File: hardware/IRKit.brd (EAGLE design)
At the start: 54 x 56 mm, 71 parts, among them CN1 USB-CONNECTORMICROB, IC1 ATMEGA32U4AU, IC2 TLV70233DBVT, IC3 LM386MM-1, IC4 GS1011MXXS, SW1 EVQPUJ02K, T1 2SD1781K, T2 BSS138

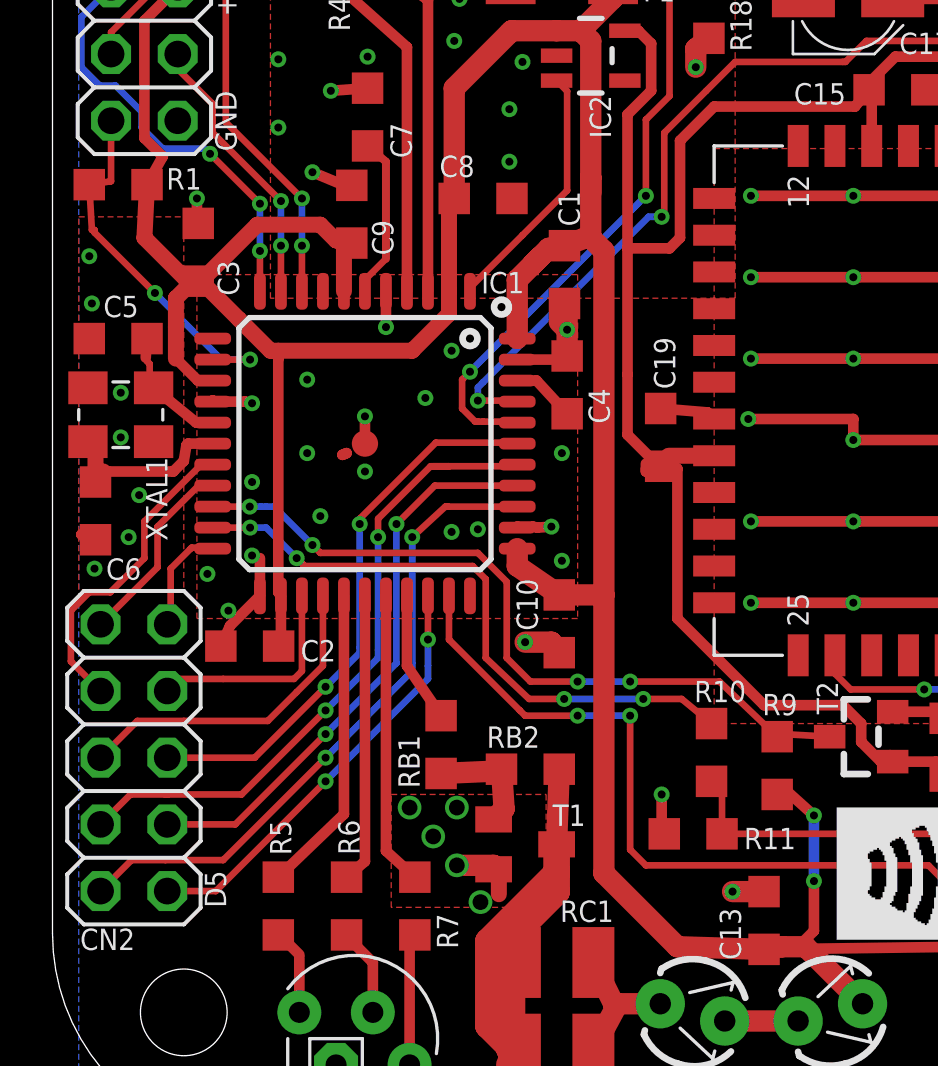
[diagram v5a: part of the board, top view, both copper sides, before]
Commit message: crystal should use the exact recommended board pattern
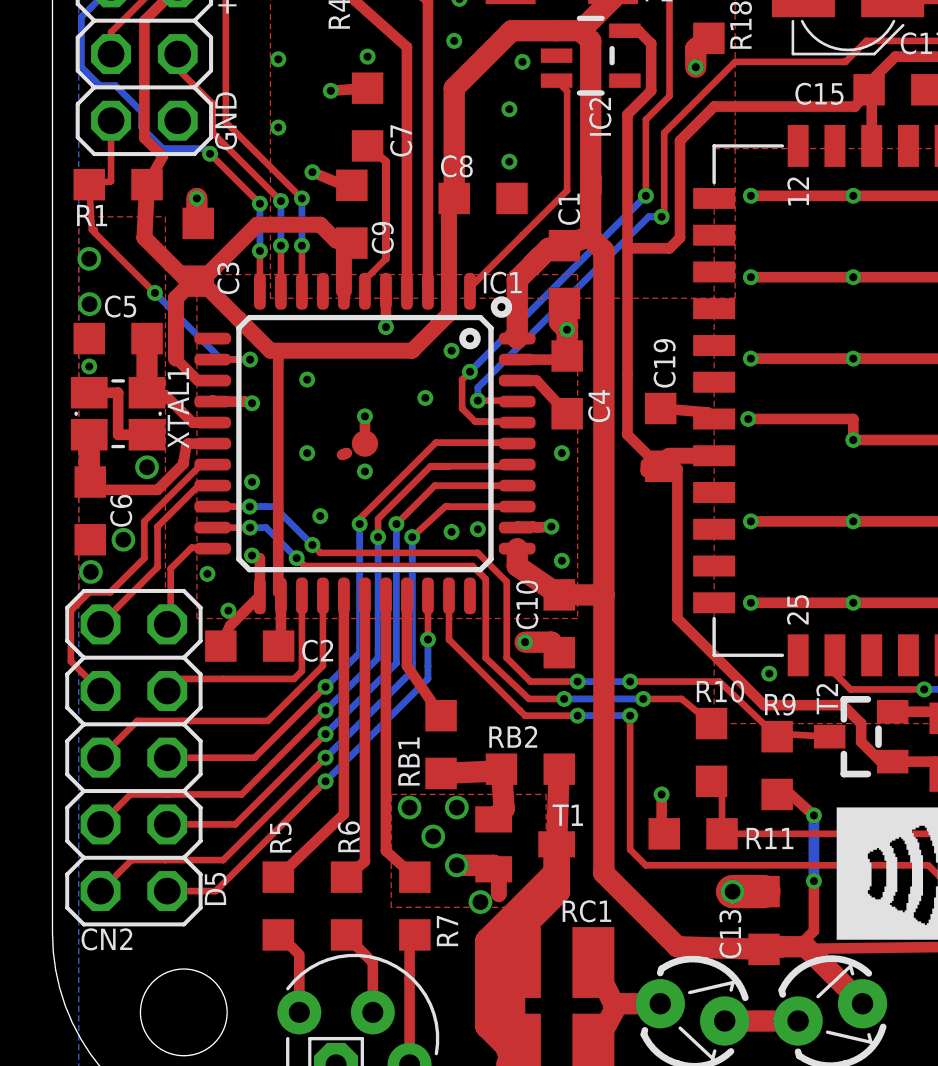
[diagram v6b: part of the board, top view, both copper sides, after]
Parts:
- moved C6 0.20 mm to (1.44, 24.1)
- moved XTAL1 0.11 mm to (2.50, 27.8)
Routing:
- net GND: track 187.2 -> 190.6 mm
- net XTAL2: track 7.30 -> 7.91 mm
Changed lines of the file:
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@@
 </element>
 <element name="R1" library="my" package="SMD2012" value="10k" x="2.5" y="36.525" smashed="yes">
-<attribute name="NAME" x="4.338" y="36.341" size="0.8128" layer="25"/>
+<attribute name="NAME" x="0.838" y="34.941" size="0.8128" layer="25"/>
 <attribute name="VALUE" x="0.638" y="35.739" size="0.8128" layer="27"/>
 </element>
@@
 <attribute name="VALUE" x="1.738" y="28.3765" size="0.8128" layer="27"/>
 </element>
-<element name="C6" library="my" package="SMD2012" value="22pF" x="1.6375" y="24.1" smashed="yes" rot="R90">
-<attribute name="NAME" x="2.038" y="21.4785" size="0.8128" layer="25"/>
-<attribute name="VALUE" x="3.9235" y="23.338" size="0.8128" layer="27" rot="R90"/>
+<element name="C6" library="my" package="SMD2012" value="22pF" x="1.4375" y="24.1" smashed="yes" rot="R90">
+<attribute name="NAME" x="3.0215" y="23.438" size="0.8128" layer="25" rot="R90"/>
+<attribute name="VALUE" x="3.7235" y="23.338" size="0.8128" layer="27" rot="R90"/>
 </element>
 <element name="C14" library="my" package="SMD2012" value="4.7uF" x="43.45" y="6.65" smashed="yes" rot="R180">
@@
 <attribute name="NAME" x="22.495" y="43.505" size="0.8128" layer="25"/>
 <attribute name="VALUE" x="17.495" y="41.925" size="1.27" layer="27"/>
-</element>
-<element name="XTAL1" library="my" package="CRYSTAL-3.2-2.5" value="16MHz" x="2.6" y="27.7625" smashed="yes">
-<attribute name="NAME" x="3.5625" y="26.15" size="0.8128" layer="25" rot="R270"/>
-<attribute name="VALUE" x="1" y="25.5125" size="0.8128" layer="27"/>
 </element>
 <element name="R10" library="my" package="SMD2012" value="2.2k" x="25.1" y="14.9" smashed="yes" rot="R90">
@@
 <attribute name="NAME" x="15.9" y="49.2" size="0.8128" layer="25"/>
 <attribute name="VALUE" x="15.9" y="46.6" size="1.016" layer="27"/>
+</element>
+<element name="XTAL1" library="my" package="CRYSTAL-3.2-2.5" value="16MHz" x="2.5" y="27.8" smashed="yes">
+<attribute name="NAME" x="5.2" y="26.45" size="0.8128" layer="25" rot="R90"/>
+<attribute name="VALUE" x="0.9" y="25.55" size="1.27" layer="27"/>
 </element>
 </elements>
@@
 <contactref element="ICSP" pad="6"/>
 <contactref element="IR-RECEIVER" pad="2"/>
-<polygon width="0.4064" layer="16" isolate="0.254">
+<polygon width="0.8128" layer="16" isolate="0.254">
 <vertex x="1" y="1"/>
 <vertex x="1" y="55"/>
@@
 <contactref element="CN1" pad="S5"/>
 <contactref element="CN1" pad="S6"/>
-<contactref element="XTAL1" pad="2"/>
 <via x="11.9" y="27.7" extent="1-16" drill="0.3048"/>
 <wire x1="11.9" y1="26.6625" x2="11.9" y2="27.7" width="0.4064" layer="1"/>
@@
 <contactref element="IC1" pad="43"/>
 <contactref element="C6" pad="1"/>
-<contactref element="XTAL1" pad="4"/>
 <contactref element="C11" pad="2"/>
 <contactref element="C14" pad="2"/>
 <wire x1="21.5" y1="51.8" x2="21.3" y2="51.7" width="0.4064" layer="1"/>
 <wire x1="24.9" y1="52" x2="24.996" y2="52.0735" width="0.4064" layer="1"/>
-<wire x1="1.5" y1="23.3" x2="1.6375" y2="23" width="0.4064" layer="1"/>
+<wire x1="1.5" y1="23.3" x2="1.4375" y2="23" width="0.4064" layer="1"/>
 <wire x1="25.2" y1="52" x2="24.996" y2="52.0735" width="0.4064" layer="1"/>
-<via x="2.9" y="23.1" extent="1-16" drill="0.3048"/>
+<via x="2.7" y="23" extent="1-16" drill="0.6"/>
 <wire x1="18.4625" y1="23.4625" x2="19" y2="23.5" width="0.4064" layer="1"/>
 <wire x1="18.3" y1="23.5" x2="17.7" y2="23.5" width="0.4064" layer="1"/>
@@
 <wire x1="11.1" y1="36.5" x2="9.9" y2="37" width="0.4064" layer="1"/>
 <wire x1="12" y1="40.2" x2="10.6" y2="40.1" width="0.4064" layer="1"/>
-<wire x1="1.5" y1="23.3" x2="1.6375" y2="23" width="0.4064" layer="1"/>
-<polygon width="0.4064" layer="1">
+<wire x1="1.5" y1="23.3" x2="1.4375" y2="23" width="0.4064" layer="1"/>
+<polygon width="0.8128" layer="1">
 <vertex x="1" y="35.3"/>
-<vertex x="5" y="35.3"/>
-<vertex x="5" y="21.1"/>
+<vertex x="4.3" y="35.3"/>
+<vertex x="4.3" y="21.1"/>
 <vertex x="1" y="21.1"/>
 </polygon>
-<via x="1.4" y="33.8" extent="1-16" drill="0.3048"/>
-<via x="1.5" y="32" extent="1-16" drill="0.3048"/>
-<via x="2.6" y="26.9" extent="1-16" drill="0.3048"/>
-<via x="3.3" y="24.7" extent="1-16" drill="0.3048"/>
-<via x="1.6" y="21.9" extent="1-16" drill="0.3048"/>
+<via x="1.4" y="33.7" extent="1-16" drill="0.6"/>
+<via x="1.4125" y="31.975" extent="1-16" drill="0.6"/>
+<via x="1.4625" y="21.775" extent="1-16" drill="0.6"/>
 <polygon width="0.4064" layer="1" isolate="0.254">
 <vertex x="5.5" y="33.1"/>
@@
 <wire x1="19.6" y1="30" x2="19.4625" y2="29.8625" width="0.8128" layer="1"/>
 <wire x1="19.4625" y1="29.8625" x2="17.7" y2="29.8625" width="0.4064" layer="1"/>
-<wire x1="1.1" y1="23.2" x2="1.6375" y2="23" width="0.4064" layer="1"/>
-<wire x1="1.1" y1="23.2" x2="1.6375" y2="23" width="0.4064" layer="1"/>
+<wire x1="1.1" y1="23.2" x2="1.4375" y2="23" width="0.4064" layer="1"/>
+<wire x1="1.1" y1="23.2" x2="1.4375" y2="23" width="0.4064" layer="1"/>
 <via x="5.5" y="36" extent="1-16" drill="0.3048"/>
-<wire x1="5.5" y1="36" x2="5.5" y2="35" width="0.4064" layer="1"/>
 <wire x1="5.5" y1="35" x2="5.55" y2="35.05" width="0.4064" layer="1"/>
 <wire x1="19.5" y1="32" x2="19.6" y2="31.8" width="0.8128" layer="1"/>
@@
 <wire x1="42.4" y1="20.6" x2="42.2" y2="20.6" width="0.4064" layer="1"/>
 <via x="17.9" y="41.2" extent="1-16" drill="0.3048"/>
-<via x="2.6" y="28.6" extent="1-16" drill="0.3048"/>
 <contactref element="R16" pad="1"/>
 <contactref element="R18" pad="2"/>
@@
 <contactref element="C13" pad="2"/>
 <contactref element="V3" pad="2"/>
-<via x="25.9" y="9.6" extent="1-16" drill="0.3048"/>
+<via x="25.9" y="9.6" extent="1-16" drill="0.6"/>
 <wire x1="18" y1="19.1" x2="19" y2="19.1" width="0.8128" layer="1"/>
 <wire x1="19" y1="19.1" x2="19.3" y2="18.7" width="0.8128" layer="1"/>
@@
 <wire x1="42.9" y1="7" x2="42.35" y2="6.65" width="0.4064" layer="1"/>
 <via x="15.4" y="12.8" extent="1-16" drill="0.6"/>
-<wire x1="25.9" y1="9.6" x2="27.1" y2="9.6" width="0.8128" layer="1"/>
 <via x="23.2" y="13.3" extent="1-16" drill="0.3048"/>
 <wire x1="23.3" y1="11.8" x2="23.2" y2="12.1" width="0.4064" layer="1"/>
@@
 <via x="16.3" y="9.2" extent="1-16" drill="0.6"/>
 <via x="14.5" y="11.7" extent="1-16" drill="0.6"/>
+<via x="3.6" y="25.7625" extent="1-16" drill="0.6"/>
+<contactref element="XTAL1" pad="2"/>
+<contactref element="XTAL1" pad="4"/>
+<via x="1.4" y="29.6" extent="1-16" drill="0.3048"/>
+<wire x1="5.5" y1="35" x2="5.5" y2="36" width="0.8128" layer="1"/>
+<wire x1="27.1" y1="9.6" x2="25.9" y2="9.6" width="1.27" layer="1"/>
+<via x="27.3" y="17.9" extent="1-16" drill="0.3048"/>
+<wire x1="1.4" y1="28.6" x2="2.5" y2="28.6" width="0.4064" layer="1"/>
+<wire x1="2.5" y1="28.6" x2="2.5" y2="27" width="0.4064" layer="1"/>
+<wire x1="2.5" y1="27" x2="3.6" y2="27" width="0.4064" layer="1"/>
 </signal>
 <signal name="N$10">
@@
 </signal>
 <signal name="XTAL1">
-<contactref element="XTAL1" pad="3"/>
 <contactref element="C5" pad="2"/>
 <contactref element="IC1" pad="16"/>
-<wire x1="6.1" y1="27.4625" x2="5.475" y2="27.4625" width="0.4064" layer="1"/>
-<wire x1="5.475" y1="27.4625" x2="3.85" y2="28.7875" width="0.4064" layer="1"/>
-<wire x1="3.55" y1="29.9375" x2="3.6" y2="30.6625" width="0.4064" layer="1"/>
-<wire x1="3.7" y1="29.7" x2="3.6" y2="29.8" width="0.254" layer="1"/>
-<wire x1="3.7" y1="28.9" x2="3.7" y2="29.7" width="0.254" layer="1"/>
-<wire x1="3.6" y1="29.8" x2="3.6" y2="30.6625" width="0.254" layer="1"/>
-<wire x1="3.7" y1="28.9" x2="3.85" y2="28.7875" width="0.254" layer="1"/>
+<contactref element="XTAL1" pad="3"/>
+<wire x1="3.6" y1="30.6625" x2="3.6" y2="28.7" width="0.8128" layer="1"/>
+<wire x1="3.6" y1="28.7" x2="3.6" y2="28.6" width="0.8128" layer="1"/>
+<wire x1="6.1" y1="27.4625" x2="5.3375" y2="27.4625" width="0.4064" layer="1"/>
+<wire x1="5.3375" y1="27.4625" x2="4.3" y2="28.5" width="0.4064" layer="1"/>
+<wire x1="4.3" y1="28.5" x2="3.8" y2="28.5" width="0.4064" layer="1"/>
+<wire x1="3.8" y1="28.5" x2="3.6" y2="28.6" width="0.4064" layer="1"/>
 </signal>
 <signal name="XTAL2">
 <contactref element="C6" pad="2"/>
 <contactref element="IC1" pad="17"/>
-<contactref element="XTAL1" pad="1"/>
 <wire x1="6.1" y1="26.6625" x2="5.1625" y2="26.6625" width="0.4064" layer="1"/>
 <wire x1="5.1625" y1="26.6625" x2="5.1" y2="26.6" width="0.4064" layer="1"/>
 <wire x1="5.1" y1="26.6" x2="5" y2="26" width="0.4064" layer="1"/>
-<wire x1="5" y1="26" x2="4.6" y2="25.6" width="0.4064" layer="1"/>
-<wire x1="4.6" y1="25.6" x2="1.9375" y2="25.6" width="0.4064" layer="1"/>
-<wire x1="1.35" y1="26.7375" x2="1.6375" y2="26.45" width="0.6096" layer="1"/>
-<wire x1="1.6375" y1="26.45" x2="1.6375" y2="25.2" width="0.6096" layer="1"/>
-<wire x1="1.9375" y1="25.6" x2="1.6" y2="25.2625" width="0.6096" layer="1"/>
-<wire x1="1.7" y1="25.1" x2="1.6375" y2="25.2" width="0.254" layer="1"/>
-<wire x1="1.7" y1="25.1" x2="1.6" y2="25.2625" width="0.254" layer="1"/>
+<wire x1="1.7375" y1="25.1" x2="1.4375" y2="25.2" width="0.4064" layer="1"/>
+<contactref element="XTAL1" pad="1"/>
+<wire x1="5" y1="26" x2="5" y2="25.9" width="0.4064" layer="1"/>
+<wire x1="5" y1="25.9" x2="4" y2="24.9" width="0.4064" layer="1"/>
+<wire x1="4" y1="24.9" x2="1.9375" y2="24.9" width="0.4064" layer="1"/>
+<wire x1="1.9375" y1="24.9" x2="1.4375" y2="25.2" width="0.4064" layer="1"/>
+<wire x1="1.4" y1="27" x2="1.4" y2="25.4375" width="0.8128" layer="1"/>
+<wire x1="1.4" y1="25.4375" x2="1.4375" y2="25.2" width="0.8128" layer="1"/>
 </signal>
 <signal name="D7/LDO3.3_EN">
@@
 <wire x1="38" y1="45.9" x2="38.5" y2="45.9" width="0.4064" layer="1"/>
 </signal>
+<signal name="N$15">
+</signal>
 </signals>
